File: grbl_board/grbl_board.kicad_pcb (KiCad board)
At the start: 4 copper layers, 138.4 x 138.3 mm, 256 parts, among them J1 COOL, J10 DOOR, J11 PROBE, J12 INP, J13 LIM, J14 24V_VFD, J15 Spindle, J16 freq, J17 USB_B, J18 ICSP, J2 12VDC, J3 USB_B, J4 ICSP, J5 Screw_Terminal_01x04, J6 X_STEPPER, J7 Y_STEPPER, J8 Z_STEPPER, J9 E_STEPPER, Q1 BSS127S, Q2 BSS127S, Q3 ZVN4306GTA, Q4 IRF9Z24SPBF, Q5 BSS127S, Q6 BSS127S, Q7 BSS127S, SW1 SW_Push, SW2 SW_Push, U1 FT231XS, U10 6N137, U11 6N137, U12 6N137, U13 6N137, U14 6N137, U15 6N137, U16 6N137, U17 6N137, U18 6N137, U19 6N137, U2 ATmega2560-16AU, U20 6N137, U21 BD9G341EFJ, U22 LMV358, U23 OPA2192, U24 L7805, U25 FT231XS, U26 40106, U27 74LS155, U28 ATmega328P-AU, U29 74LS153, U3 L7805, U30 74LS153, U31 LMV358, U4 BD9G341EFJ, U5 TMC5160_SILENTSTEPSTICK, U6 TMC5160_SILENTSTEPSTICK, U7 TMC5160_SILENTSTEPSTICK, U8 TMC5160_SILENTSTEPSTICK, U9 6N137, Y1 16M, Y2 16M

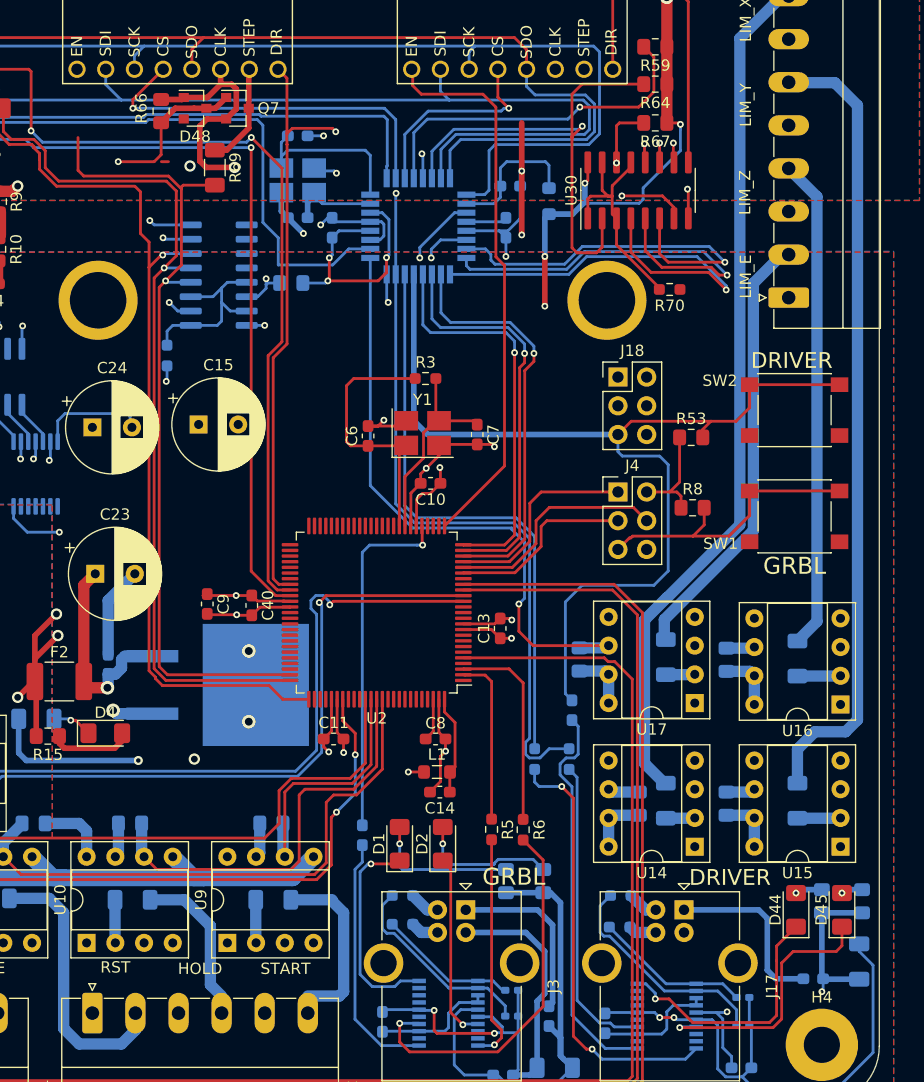
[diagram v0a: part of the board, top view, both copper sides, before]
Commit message: added limit switch indicator LEDs
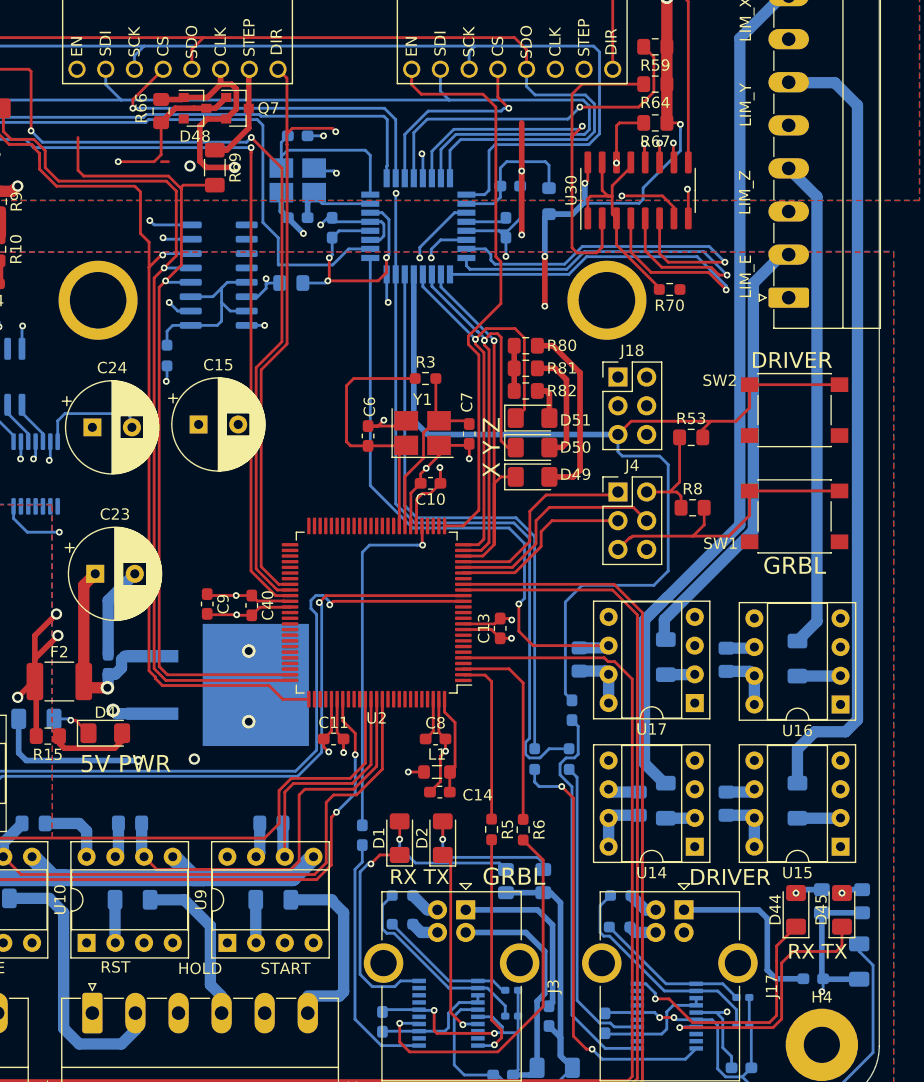
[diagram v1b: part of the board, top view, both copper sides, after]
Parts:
- added D49: LED, LED_SMD:LED_1206_3216Metric_Pad1.42x1.75mm_HandSolder, F.Cu at (180.6, 105.6)
- added D50: LED, LED_SMD:LED_1206_3216Metric_Pad1.42x1.75mm_HandSolder, F.Cu at (180.6, 103.0)
- added D51: LED, LED_SMD:LED_1206_3216Metric_Pad1.42x1.75mm_HandSolder, F.Cu at (180.6, 100.4)
- added R80: 270, Resistor_SMD:R_0805_2012Metric_Pad1.15x1.40mm_HandSolder, F.Cu at (180.0, 94.0)
- added R81: 270, Resistor_SMD:R_0805_2012Metric_Pad1.15x1.40mm_HandSolder, F.Cu at (180.0, 96.0)
- added R82: 270, Resistor_SMD:R_0805_2012Metric_Pad1.15x1.40mm_HandSolder, F.Cu at (180.0, 98.0)
- moved C7 0.71 mm to (175.0, 101.8)
- moved D1 0.50 mm to (168.8, 137.5)
- moved D2 0.50 mm to (172.7, 137.5)
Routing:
- net Net-(D49-Pad2): track 0.00 -> 16.3 mm
- net Net-(D50-Pad2): track 0.00 -> 10.3 mm
- net /grbl_controller/LIM_Y: track 35.8 -> 41.0 mm
- net /grbl_controller/LIM_Z: track 35.2 -> 40.1 mm
- net /grbl_controller/5VDC: track 0.00 -> 4.00 mm
- net Net-(D51-Pad2): track 0.00 -> 3.29 mm
- net /stepper_drivers/EN: track 140.9 -> 142.4 mm
- net Net-(D1-Pad2): track 13.0 -> 12.0 mm
- net GND: track 704.7 -> 703.8 mm
- net /grbl_controller/DIR_Y: track 115.1 -> 115.9 mm
- net /grbl_controller/DIR_Z: track 81.8 -> 82.7 mm
- net Net-(D2-Pad2): track 12.6 -> 11.9 mm
- net Net-(C7-Pad1): track 18.1 -> 17.4 mm
- net Net-(D2-Pad1): track 16.6 -> 17.1 mm
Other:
- board text added: "5V PWR"
- board text added: "RX TX"
- board text added: "X Y Z"

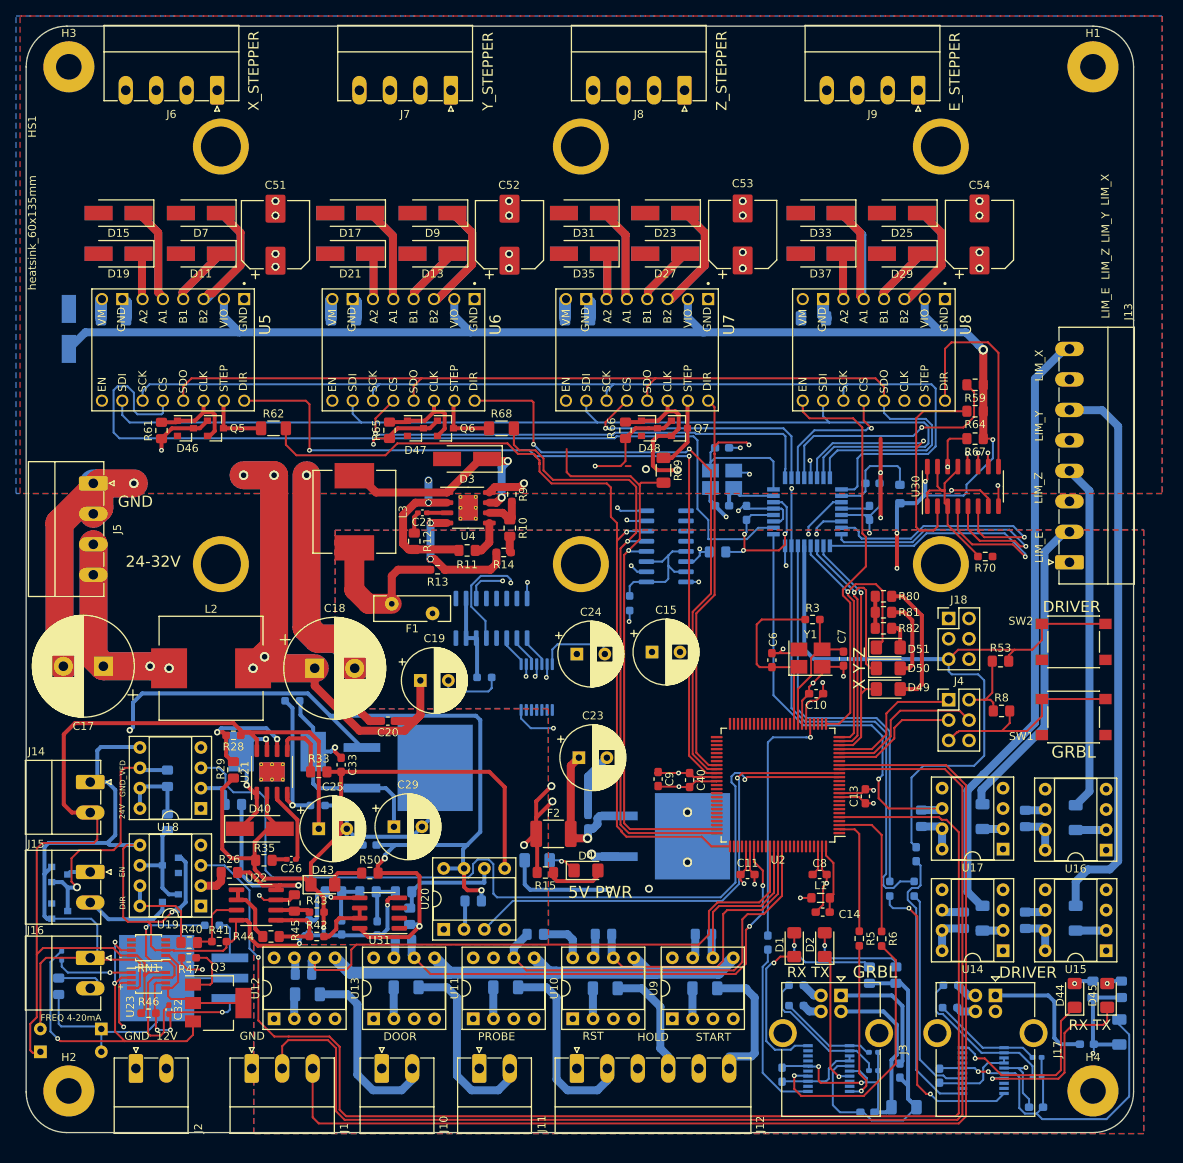
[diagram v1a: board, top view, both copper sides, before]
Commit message: updated board with 24V reg
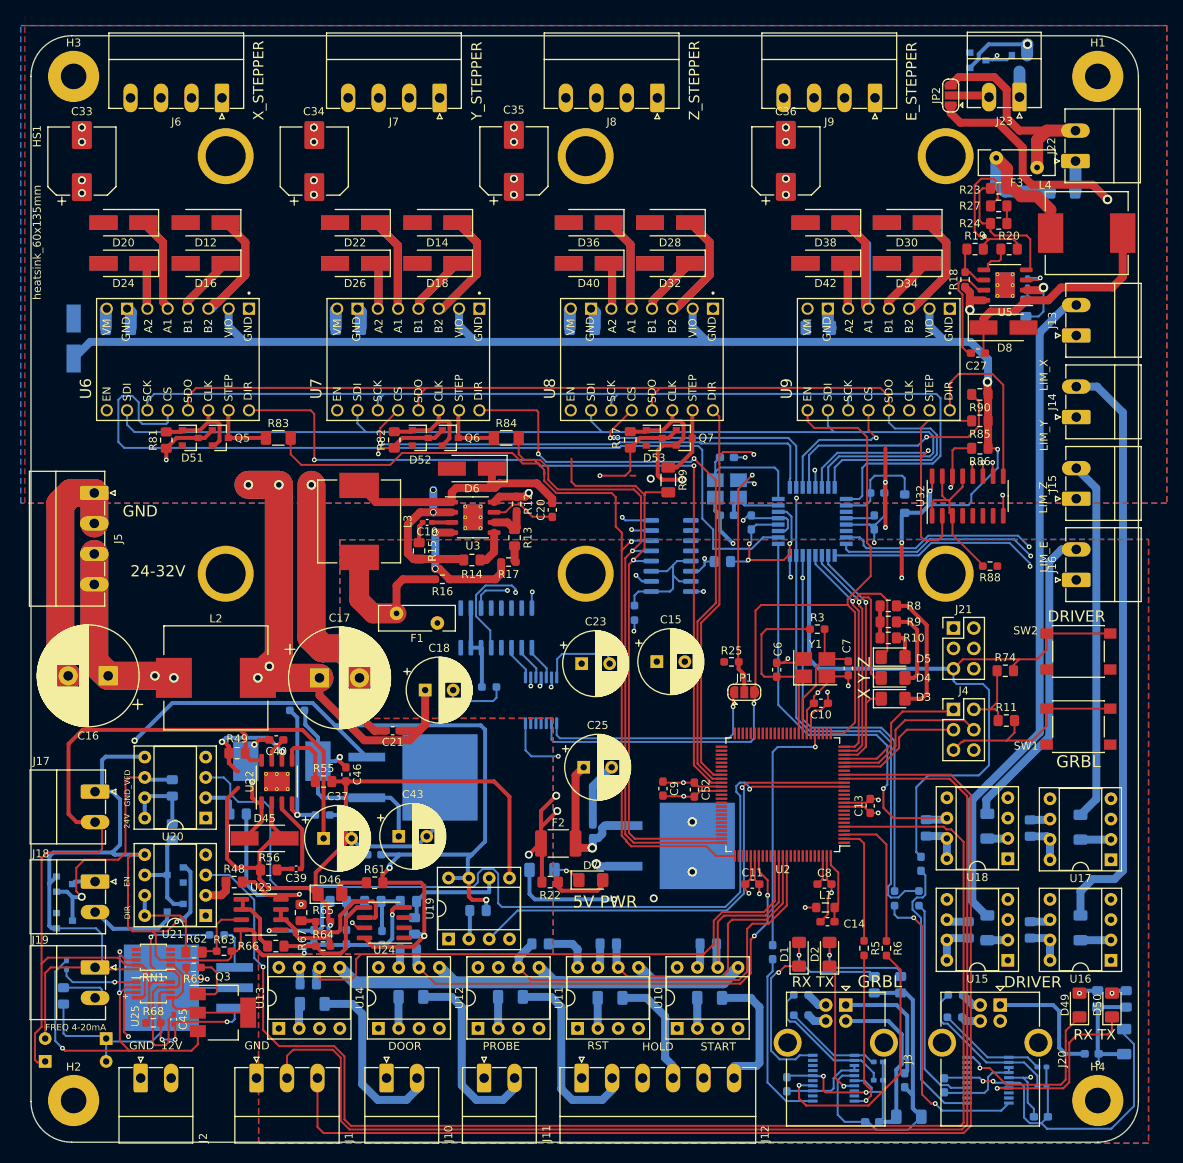
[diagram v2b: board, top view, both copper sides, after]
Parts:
- removed the R28 at (98.7, 111.4)
- removed the R29 at (98.7, 115.7)
- removed the U26 at (136.7, 105.3)
- removed the U31 at (117.0, 133.6)
- added C20: 100n, Capacitor_SMD:C_0603_1608Metric_Pad1.05x0.95mm_HandSolder, F.Cu at (138.6, 83.2)
- added C26: 6.8n, Capacitor_SMD:C_0402_1005Metric_Pad0.74x0.62mm_HandSolder, B.Cu at (198.0, 54.8)
- added C27: 100n, Capacitor_SMD:C_0603_1608Metric_Pad1.05x0.95mm_HandSolder, F.Cu at (191.8, 63.6)
- added C28: 1u, Capacitor_SMD:C_1206_3216Metric_Pad1.33x1.80mm_HandSolder, B.Cu at (202.4, 43.4)
- added C40: 100n, Capacitor_SMD:C_0603_1608Metric_Pad1.05x0.95mm_HandSolder, F.Cu at (104.1, 112.0)
- added D8: SS2150-LTP, Diode_SMD:D_SMA_Handsoldering, F.Cu at (195.0, 60.4)
- added D9: BZX84C5V6, Diode_SMD:D_SOT-23_ANK, B.Cu at (191.8, 27.0)
- added F3: 2A, Fuse:Fuse_Bourns_MF-RHT200, F.Cu at (199.2, 40.4)
- added J14: LIM_Y, Connector_Phoenix_MC:PhoenixContact_MC_1,5_2-G-3.81_1x02_P3.81mm_Horizontal, F.Cu at (204.1, 71.6)
- added J15: LIM_Z, Connector_Phoenix_MC:PhoenixContact_MC_1,5_2-G-3.81_1x02_P3.81mm_Horizontal, F.Cu at (204.1, 81.8)
- added J16: LIM_E, Connector_Phoenix_MC:PhoenixContact_MC_1,5_2-G-3.81_1x02_P3.81mm_Horizontal, F.Cu at (204.1, 92.0)
- added J22: 24VDC, Connector_Phoenix_MC:PhoenixContact_MC_1,5_2-G-3.81_1x02_P3.81mm_Horizontal, F.Cu at (204.0, 39.6)
- added J23: BRAKE, Connector_Phoenix_MC:PhoenixContact_MC_1,5_2-G-3.81_1x02_P3.81mm_Horizontal, F.Cu at (197.0, 31.6)
- added JP1: SolderJumper_3_Open, Jumper:SolderJumper-3_P1.3mm_Open_RoundedPad1.0x1.5mm, F.Cu at (162.6, 106.0)
- added JP2: SolderJumper_3_Open, Jumper:SolderJumper-3_P1.3mm_Open_RoundedPad1.0x1.5mm, F.Cu at (188.4, 31.4)
- added L4: 33u, Inductor_SMD:L_Vishay_IHLP-4040, F.Cu at (205.4, 48.6)
- added Q8: SSM3K361R,LF, Package_TO_SOT_SMD:SOT-23, B.Cu at (197.0, 27.4)
- added R18: 100k, Resistor_SMD:R_0603_1608Metric_Pad0.98x0.95mm_HandSolder, F.Cu at (190.2, 54.4)
- added R19: 10k, Resistor_SMD:R_0805_2012Metric_Pad1.15x1.40mm_HandSolder, F.Cu at (191.4, 50.6)
- added R20: 47k, Resistor_SMD:R_0805_2012Metric_Pad1.15x1.40mm_HandSolder, F.Cu at (195.7, 50.6)
- added R21: 10k, Resistor_SMD:R_0805_2012Metric_Pad1.15x1.40mm_HandSolder, B.Cu at (197.8, 58.0)
- added R23: 12k, Resistor_SMD:R_0805_2012Metric_Pad1.15x1.40mm_HandSolder, F.Cu at (194.4, 43.0)
- added R24: 270, Resistor_SMD:R_0805_2012Metric_Pad1.15x1.40mm_HandSolder, F.Cu at (194.4, 47.4)
- added R25: 2.2k, Resistor_SMD:R_0603_1608Metric_Pad0.98x0.95mm_HandSolder, F.Cu at (161.0, 102.2)
- added R27: 270, Resistor_SMD:R_0805_2012Metric_Pad1.15x1.40mm_HandSolder, F.Cu at (194.4, 45.2)
- added R49: 10k, Resistor_SMD:R_0805_2012Metric_Pad1.15x1.40mm_HandSolder, F.Cu at (99.2, 113.6)
- added U24: LMV358, Package_SO:SOIC-8_3.9x4.9mm_P1.27mm, F.Cu at (117.6, 134.8)
- added U28: 40106, Package_SO:TSSOP-14_4.4x5mm_P0.65mm, B.Cu at (137.2, 107.0)
- added U5: BD9G341EFJ, Package_SO:HTSOP-8-1EP_3.9x4.9mm_P1.27mm_EP2.4x3.2mm_ThermalVias, F.Cu at (195.2, 55.1)
- J13: value LIM -> LIM_X; footprint Connector_Phoenix_MC:PhoenixContact_MC_1,5_8-G-3.81_1x08_P3.81mm_Horizontal -> Connector_Phoenix_MC:PhoenixContact_MC_1,5_2-G-3.81_1x02_P3.81mm_Horizontal
- moved C35 30.0 mm to (133.8, 39.6)
- moved J13 28.4 mm to (204.1, 61.4)
- moved C34 26.1 mm to (108.8, 39.6)
- moved C33 25.9 mm to (79.8, 39.6)
- moved C36 25.9 mm to (167.8, 39.6)
- moved J9 5.48 mm to (178.9, 31.7)
- moved J8 3.53 mm to (151.7, 31.7)
- moved J7 1.69 mm to (124.5, 31.7)
- moved D46 1.49 mm to (110.8, 131.2)
- moved R67 1.46 mm to (107.2, 133.5)
- moved R64 1.44 mm to (110.0, 137.7)
- moved R65 1.44 mm to (110.0, 134.7)
- moved C5 1.34 mm to (167.9, 155.0)
- moved C54 1.34 mm to (199.7, 159.1)
- moved FB1 1.34 mm to (182.7, 154.5)
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- renumbered C17 to C16, C18 to C17, C19 to C18, C21 to C19, C20 to C21, C16 to C22, C24 to C23, C22 to C24, C23 to C25, C47 to C29, C48 to C30, C49 to C31, C50 to C32, C51 to C33, C52 to C34, C53 to C35, C54 to C36, C25 to C37, C27 to C38, C26 to C39, C28 to C41, C30 to C42, C29 to C43, C31 to C44, C32 to C45, C33 to C46, C34 to C47, C35 to C48, C36 to C49, C37 to C50, C38 to C51, C40 to C52, C39 to C53, C41 to C54, C42 to C55, C43 to C56, C44 to C57, C45 to C58, C46 to C59, D5 to D10, D6 to D11, D7 to D12, D8 to D13, D9 to D14, D10 to D15, D11 to D16, D12 to D17, D13 to D18, D14 to D19, D15 to D20, D16 to D21, D17 to D22, D18 to D23, D19 to D24, D20 to D25, D21 to D26, D22 to D27, D23 to D28, D24 to D29, D49 to D3, D25 to D30, D26 to D31, D27 to D32, D28 to D33, D29 to D34, D30 to D35, D31 to D36, D32 to D37, D33 to D38, D34 to D39, D50 to D4, D35 to D40, D36 to D41, D37 to D42, D38 to D43, D39 to D44, D40 to D45, D43 to D46, D41 to D47, D42 to D48, D44 to D49, D51 to D5, D45 to D50, D46 to D51, D47 to D52, D48 to D53, D3 to D6, D4 to D7, J14 to J17, J15 to J18, J16 to J19, J17 to J20, J18 to J21, L4 to L5, L5 to L6, R82 to R10, R8 to R11, R9 to R12, R10 to R13, R11 to R14, R12 to R15, R13 to R16, R14 to R17, R15 to R22, R16 to R28, R17 to R29, R18 to R30, R19 to R31, R20 to R32, R31 to R33, R32 to R34, R71 to R35, R72 to R36, R73 to R37, R21 to R38, R22 to R39, R23 to R40, R24 to R41, R74 to R42, R75 to R43, R76 to R44, R77 to R45, R27 to R46, R25 to R47, R26 to R48, R30 to R51, R78 to R52, R79 to R53, R34 to R54, R33 to R55, R35 to R56, R36 to R57, R37 to R58, R38 to R59, R39 to R60, R50 to R61, R40 to R62, R41 to R63, R42 to R64, R43 to R65, R44 to R66, R45 to R67, R46 to R68, R47 to R69, R48 to R70, R49 to R71, R51 to R72, R52 to R73, R53 to R74, R54 to R75, R55 to R76, R56 to R77, R57 to R78, R58 to R79, R80 to R8, R63 to R80, R61 to R81, R65 to R82, R62 to R83, R68 to R84, R64 to R85, R67 to R86, R66 to R87, R70 to R88, R69 to R89, R81 to R9, R59 to R90, R60 to R91, U9 to U10, U10 to U11, U11 to U12, U12 to U13, U13 to U14, U14 to U15, U15 to U16, U16 to U17, U17 to U18, U20 to U19, U18 to U20, U19 to U21, U21 to U22, U22 to U23, U23 to U25, U24 to U26, U25 to U27, U27 to U29, U4 to U3, U28 to U30, U29 to U31, U30 to U32, U3 to U4, U5 to U6, U6 to U7, U7 to U8, U8 to U9
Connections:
- net /stepper_drivers/EN renamed /stepper_drivers/BRAKE
- C42 pad 1: Net-(C30-Pad1) -> Net-(C42-Pad1)
- D45 pad 1: Net-(D40-Pad1) -> Net-(C40-Pad2)
- D6 pad 1: Net-(D3-Pad1) -> Net-(C20-Pad2)
- L3 pad 1: Net-(D3-Pad1) -> Net-(C20-Pad2)
- L5 pad 1: Net-(D40-Pad1) -> Net-(C40-Pad2)
- R38 pad 2: Net-(J13-Pad8) -> Net-(J13-Pad2)
- R39 pad 2: Net-(J13-Pad6) -> Net-(J14-Pad2)
- R40 pad 2: Net-(J13-Pad4) -> Net-(J15-Pad2)
- R41 pad 2: Net-(J13-Pad2) -> Net-(J16-Pad2)
- R60 pad 1: Net-(C30-Pad1) -> Net-(C42-Pad1)
- R64 pad 1: Net-(R42-Pad1) -> Net-(R64-Pad1)
- R64 pad 2: Net-(R42-Pad2) -> Net-(R64-Pad2)
- R65 pad 1: Net-(R43-Pad1) -> Net-(R65-Pad1)
- R66 pad 2: Net-(R42-Pad1) -> Net-(R64-Pad1)
- R67 pad 1: Net-(R45-Pad1) -> Net-(R67-Pad1)
- R67 pad 2: Net-(R43-Pad1) -> Net-(R65-Pad1)
- R76 pad 1: /aux_mcu/RX0 -> /aux_mcu/EN1
- U22 pad 1: Net-(D40-Pad1) -> Net-(C40-Pad2)
- U22 pad 7: Net-(D40-Pad1) -> Net-(C40-Pad1)
- U23 pad 5: Net-(R42-Pad1) -> Net-(C42-Pad1)
- U23 pad 6: Net-(R43-Pad1) -> Net-(R64-Pad2)
- U23 pad 7: Net-(R45-Pad1) -> Net-(R64-Pad2)
- U25 pad 3: Net-(R45-Pad1) -> Net-(R67-Pad1)
- U3 pad 1: Net-(D3-Pad1) -> Net-(C20-Pad2)
- U3 pad 7: Net-(D3-Pad1) -> Net-(C20-Pad1)
- U30 pad 19: /aux_mcu/EN0 -> Net-(U30-Pad19)
- U30 pad 22: /aux_mcu/EN1 -> Net-(U30-Pad22)
- U30 pad 30: /aux_mcu/RX0 -> /aux_mcu/EN1
- U30 pad 32: /aux_mcu/LIM_0 -> /aux_mcu/EN0
- U32 pad 4: /aux_mcu/LIM_Z -> Net-(U32-Pad4)
- U32 pad 5: /aux_mcu/LIM_Y -> Net-(U32-Pad5)
- U32 pad 6: /aux_mcu/LIM_X -> Net-(U32-Pad6)
- U32 pad 7: /aux_mcu/LIM_0 -> Net-(U32-Pad7)
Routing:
- net Net-(D9-Pad1): track 0.00 -> 119.8 mm, vias 0 -> 2
- net Net-(J13-Pad8): track 75.3 -> 0.00 mm
- net Net-(J14-Pad2): track 0.00 -> 73.8 mm
- net Net-(J13-Pad6): track 71.3 -> 0.00 mm
- net /stepper_drivers/BRAKE: track 142.4 -> 197.9 mm, vias 0 -> 1
- net Net-(R67-Pad1): track 0.00 -> 55.1 mm, vias 0 -> 3
- net /aux_mcu/RX0: track 51.8 -> 0.00 mm
- net +12V: track 344.7 -> 392.0 mm, vias 2 -> 3
- net Net-(J15-Pad2): track 0.00 -> 45.2 mm
- net Net-(J13-Pad2): track 38.1 -> 83.1 mm
- net Net-(R45-Pad1): track 44.9 -> 0.00 mm, vias 2 -> 0
- net Net-(J13-Pad4): track 43.5 -> 0.00 mm
- net /aux_mcu/EN1: track 56.7 -> 97.9 mm
- net Net-(J16-Pad2): track 0.00 -> 38.5 mm
- net /aux_mcu/LIM_0: track 37.1 -> 0.00 mm, vias 2 -> 0
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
